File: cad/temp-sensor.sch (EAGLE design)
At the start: 62 parts, among them J2 455-1750-1-ND, Q1 300S14-U, Q2 320S14-U, Q3 320S14-U, U1 SE555D, U2 SE555D, U4 MCP6001UT-I/OT, U5 MCP6001UT-I/OT, U6 MCP6001UT-I/OT, U7 MCP6001UT-I/OT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

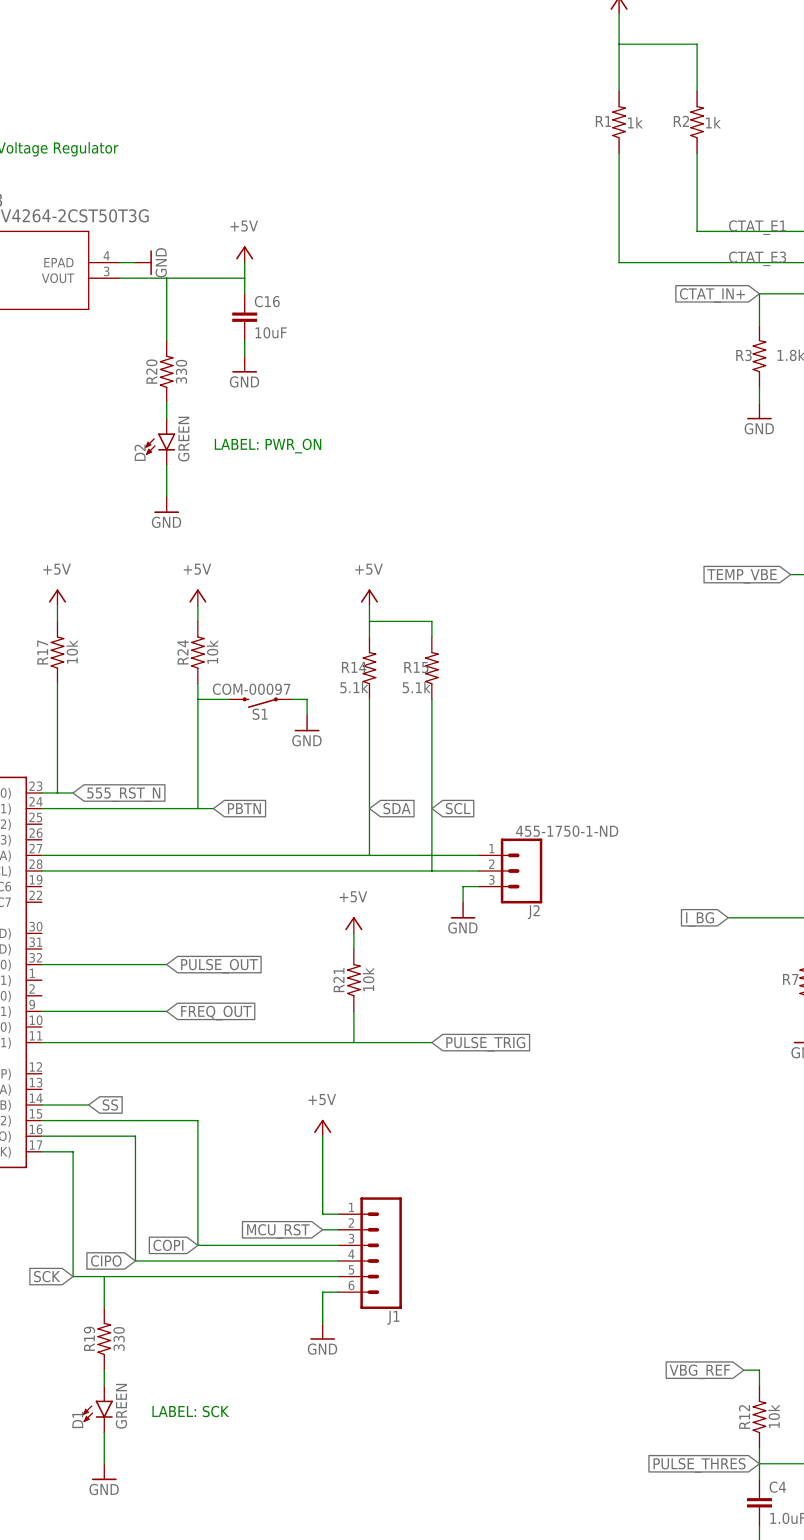
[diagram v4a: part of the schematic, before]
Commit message: Initial routing
Still need to add test points and clean up silk screen.
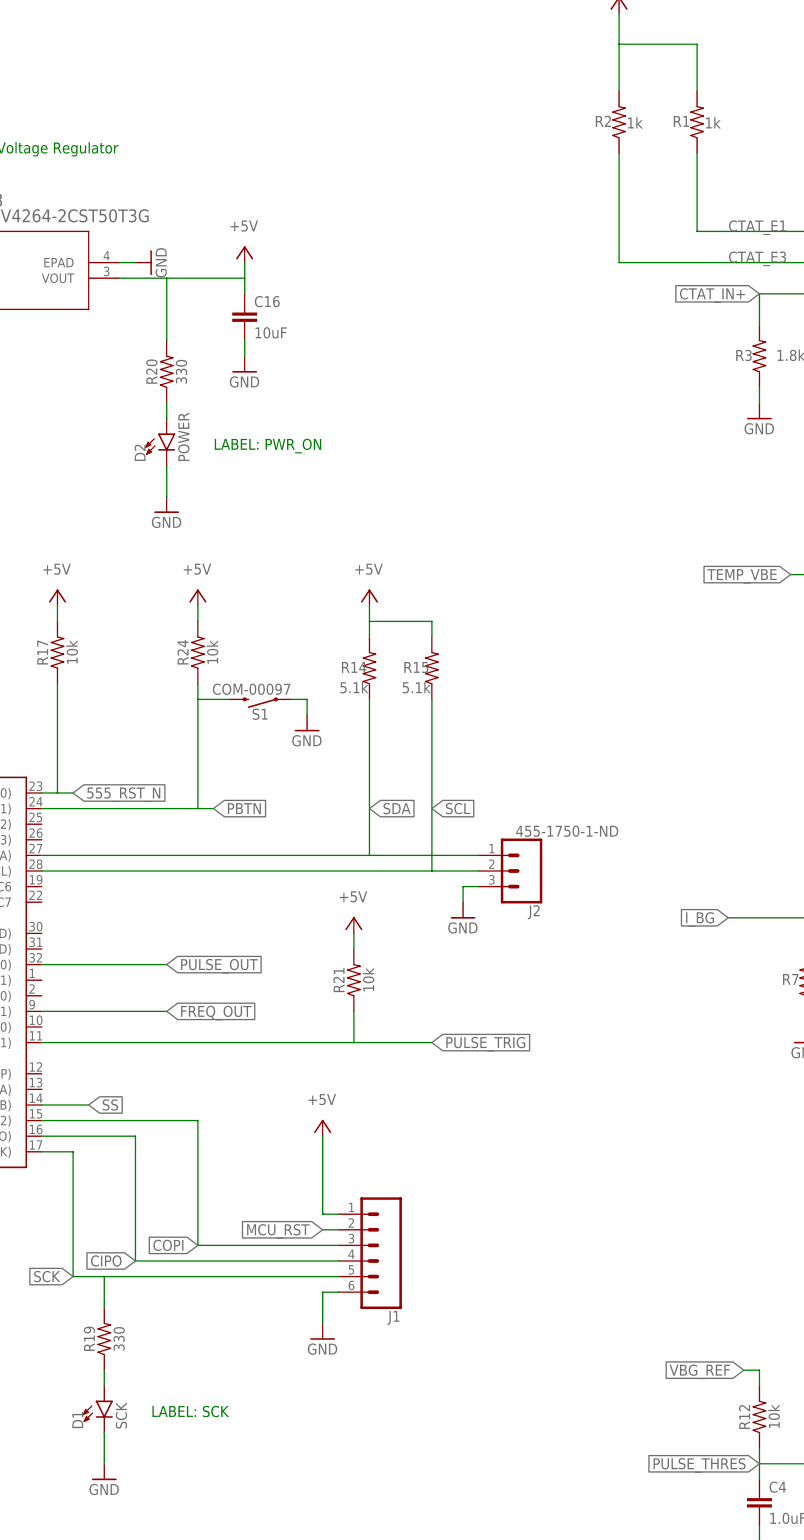
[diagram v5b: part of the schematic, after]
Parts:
- D1: value GREEN -> SCK
- D2: value GREEN -> POWER
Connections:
- net CTAT_E1: now also R1.1; no longer R2.1
- net CTAT_E3: now also R2.1; no longer R1.1
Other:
- moved on the sheet: R1, R2
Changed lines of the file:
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@@
 <part name="P+3" library="supply1" library_urn="urn:adsk.eagle:library:371" deviceset="+5V" device=""/>
 <part name="GND3" library="supply1" library_urn="urn:adsk.eagle:library:371" deviceset="GND" device=""/>
+<part name="R2" library="SparkFun-Resistors" library_urn="urn:adsk.eagle:library:532" deviceset="1KOHM" device="-0603-1/10W-1%" package3d_urn="urn:adsk.eagle:package:41389018/1" value="1k"/>
 <part name="R1" library="SparkFun-Resistors" library_urn="urn:adsk.eagle:library:532" deviceset="1KOHM" device="-0603-1/10W-1%" package3d_urn="urn:adsk.eagle:package:41389018/1" value="1k"/>
-<part name="R2" library="SparkFun-Resistors" library_urn="urn:adsk.eagle:library:532" deviceset="1KOHM" device="-0603-1/10W-1%" package3d_urn="urn:adsk.eagle:package:41389018/1" value="1k"/>
 <part name="R4" library="SparkFun-Resistors" library_urn="urn:adsk.eagle:library:532" deviceset="100KOHM" device="-0603-1/10W-1%" package3d_urn="urn:adsk.eagle:package:41389018/1" value="100k"/>
 <part name="R7" library="SparkFun-Resistors" library_urn="urn:adsk.eagle:library:532" deviceset="5.1KOHM" device="5.1KOHM-0603-1/10W-1%" package3d_urn="urn:adsk.eagle:package:41389018/1" value="5.1k"/>
@@
 <part name="P+17" library="supply1" library_urn="urn:adsk.eagle:library:371" deviceset="+5V" device=""/>
 <part name="P+18" library="supply1" library_urn="urn:adsk.eagle:library:371" deviceset="+5V" device=""/>
-<part name="D1" library="SparkFun-LED" library_urn="urn:adsk.eagle:library:529" deviceset="LED-GREEN" device="1206" package3d_urn="urn:adsk.eagle:package:39352/2" value="GREEN"/>
+<part name="D1" library="SparkFun-LED" library_urn="urn:adsk.eagle:library:529" deviceset="LED-GREEN" device="1206" package3d_urn="urn:adsk.eagle:package:39352/2" value="SCK"/>
 <part name="GND40" library="supply1" library_urn="urn:adsk.eagle:library:371" deviceset="GND" device=""/>
 <part name="R19" library="SparkFun-Resistors" library_urn="urn:adsk.eagle:library:532" deviceset="330OHM" device="-0603-1/10W-1%" package3d_urn="urn:adsk.eagle:package:41389018/1" value="330"/>
-<part name="D2" library="SparkFun-LED" library_urn="urn:adsk.eagle:library:529" deviceset="LED-GREEN" device="1206" package3d_urn="urn:adsk.eagle:package:39352/2" value="GREEN"/>
+<part name="D2" library="SparkFun-LED" library_urn="urn:adsk.eagle:library:529" deviceset="LED-GREEN" device="1206" package3d_urn="urn:adsk.eagle:package:39352/2" value="POWER"/>
 <part name="GND41" library="supply1" library_urn="urn:adsk.eagle:library:371" deviceset="GND" device=""/>
 <part name="R20" library="SparkFun-Resistors" library_urn="urn:adsk.eagle:library:532" deviceset="330OHM" device="-0603-1/10W-1%" package3d_urn="urn:adsk.eagle:package:41389018/1" value="330"/>
@@
 <attribute name="VALUE" x="78.74" y="73.66" size="1.778" layer="96"/>
 </instance>
-<instance part="R1" gate="G$1" x="-22.86" y="243.84" smashed="yes" rot="R90">
+<instance part="R2" gate="G$1" x="-22.86" y="243.84" smashed="yes" rot="R90">
 <attribute name="NAME" x="-25.4" y="244.856" size="1.778" layer="95" font="vector" rot="R180" align="bottom-center"/>
 <attribute name="VALUE" x="-20.32" y="242.824" size="1.778" layer="96" font="vector" rot="R180" align="top-center"/>
 </instance>
-<instance part="R2" gate="G$1" x="-10.16" y="243.84" smashed="yes" rot="R90">
+<instance part="R1" gate="G$1" x="-10.16" y="243.84" smashed="yes" rot="R90">
 <attribute name="NAME" x="-12.7" y="244.856" size="1.778" layer="95" font="vector" rot="R180" align="bottom-center"/>
 <attribute name="VALUE" x="-7.62" y="242.824" size="1.778" layer="96" font="vector" rot="R180" align="top-center"/>
@@
 <wire x1="-22.86" y1="256.54" x2="-22.86" y2="261.62" width="0.1524" layer="91"/>
 <wire x1="-22.86" y1="256.54" x2="-10.16" y2="256.54" width="0.1524" layer="91"/>
+<pinref part="R1" gate="G$1" pin="2"/>
+<wire x1="-10.16" y1="248.92" x2="-10.16" y2="256.54" width="0.1524" layer="91"/>
 <pinref part="R2" gate="G$1" pin="2"/>
-<wire x1="-10.16" y1="248.92" x2="-10.16" y2="256.54" width="0.1524" layer="91"/>
-<pinref part="R1" gate="G$1" pin="2"/>
 <wire x1="-22.86" y1="248.92" x2="-22.86" y2="256.54" width="0.1524" layer="91"/>
 </segment>
@@
 <wire x1="-22.86" y1="220.98" x2="33.02" y2="220.98" width="0.1524" layer="91"/>
 <label x="-5.08" y="220.98" size="1.778" layer="95"/>
-<pinref part="R1" gate="G$1" pin="1"/>
+<pinref part="R2" gate="G$1" pin="1"/>
 </segment>
 </net>
@@
 <wire x1="-10.16" y1="226.06" x2="33.02" y2="226.06" width="0.1524" layer="91"/>
 <label x="-5.08" y="226.06" size="1.778" layer="95"/>
-<pinref part="R2" gate="G$1" pin="1"/>
+<pinref part="R1" gate="G$1" pin="1"/>
 </segment>
 </net>

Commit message: Clean up silk and add test points
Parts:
- added C11, C13: 10uF, SparkFun-Capacitors:10UF-0805-25V-10%
- added TP1, TP2, TP3, TP4: TPPAD1-13, testpad:TPPAD1-13
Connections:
- net +5V: now also TP1.TP
- net GND: now also C11.2, C13.2, TP2.TP
- net VBG_REF: now also C11.1, TP3.TP
- net VPTAT_REF: now also C13.1, TP4.TP
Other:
- note added: "LABEL: POWER"
- note removed: "LABEL: PWR_ON"

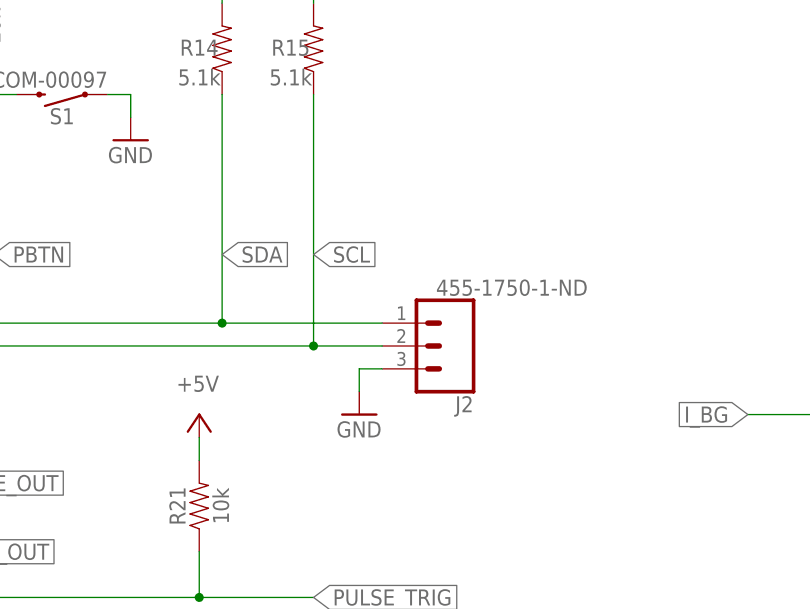
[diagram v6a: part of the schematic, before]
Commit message: Add 4 pin header for OLED
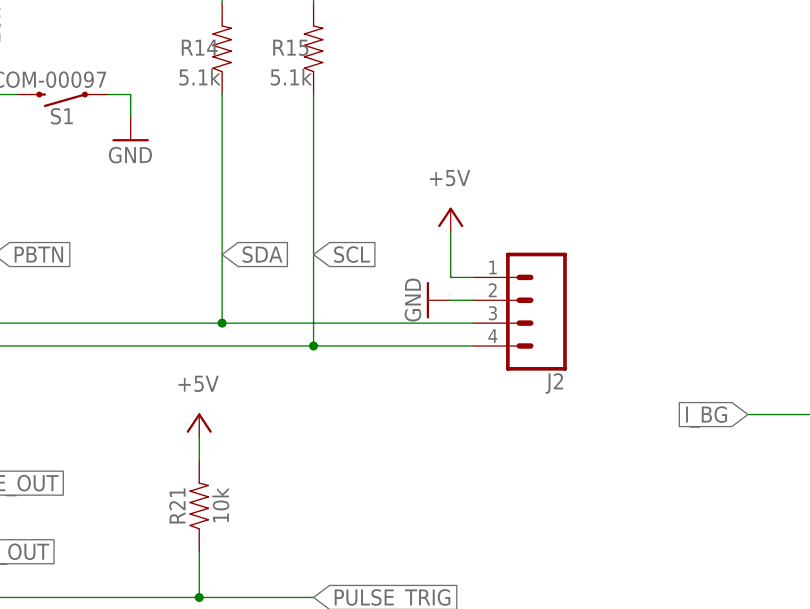
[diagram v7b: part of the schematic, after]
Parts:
- J2: value 455-1750-1-ND -> (none); device SparkFun-Connectors:CONN_03 -> SparkFun-Connectors:CONN_04PTH
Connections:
- net +5V: now also J2.1
- net GND: now also J2.2; no longer J2.3
- net SCL: now also J2.4; no longer J2.2
- net SDA: now also J2.3; no longer J2.1
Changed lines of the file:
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@@
 <part name="P+12" library="supply1" library_urn="urn:adsk.eagle:library:371" deviceset="+5V" device=""/>
 <part name="R21" library="SparkFun-Resistors" library_urn="urn:adsk.eagle:library:532" deviceset="10KOHM" device="-0603-1/10W-1%" package3d_urn="urn:adsk.eagle:package:41389018/1" value="10k"/>
-<part name="J2" library="SparkFun-Connectors" library_urn="urn:adsk.eagle:library:513" deviceset="CONN_03" device="" package3d_urn="urn:adsk.eagle:package:38063/2" value="455-1750-1-ND"/>
 <part name="GND27" library="supply1" library_urn="urn:adsk.eagle:library:371" deviceset="GND" device=""/>
 <part name="C11" library="SparkFun-Capacitors" library_urn="urn:adsk.eagle:library:510" deviceset="10UF" device="-0805-25V-10%" package3d_urn="urn:adsk.eagle:package:41385092/1" value="10uF"/>
@@
 <attribute name="TP_SIGNAL_NAME" value="VPTAT"/>
 </part>
+<part name="J2" library="SparkFun-Connectors" library_urn="urn:adsk.eagle:library:513" deviceset="CONN_04" device="PTH" package3d_urn="urn:adsk.eagle:package:38085/2"/>
+<part name="P+22" library="supply1" library_urn="urn:adsk.eagle:library:371" deviceset="+5V" device=""/>
 </parts>
 <sheets>
@@
 <attribute name="VALUE" x="-64.516" y="104.14" size="1.778" layer="96" font="vector" rot="R90" align="top-center"/>
 </instance>
-<instance part="J2" gate="J1" x="-38.1" y="121.92" smashed="yes" rot="R180">
-<attribute name="VALUE" x="-22.86" y="129.286" size="1.778" layer="96" font="vector" rot="R180"/>
-<attribute name="NAME" x="-35.56" y="116.332" size="1.778" layer="95" font="vector" rot="R180"/>
-</instance>
-<instance part="GND27" gate="1" x="-48.26" y="114.3" smashed="yes">
-<attribute name="VALUE" x="-50.8" y="111.76" size="1.778" layer="96"/>
+<instance part="GND27" gate="1" x="-40.64" y="127" smashed="yes" rot="R270">
+<attribute name="VALUE" x="-43.18" y="129.54" size="1.778" layer="96" rot="R270"/>
 </instance>
 <instance part="C11" gate="G$1" x="91.44" y="106.68" smashed="yes">
@@
 <attribute name="NAME" x="275.59" y="100.33" size="1.778" layer="95" rot="R180"/>
 <attribute name="TP_SIGNAL_NAME" x="278.13" y="102.87" size="1.778" layer="97"/>
+</instance>
+<instance part="J2" gate="J1" x="-30.48" y="127" smashed="yes" rot="R180">
+<attribute name="VALUE" x="-25.4" y="134.366" size="1.778" layer="96" font="vector" rot="R180"/>
+<attribute name="NAME" x="-25.4" y="118.872" size="1.778" layer="95" font="vector" rot="R180"/>
+</instance>
+<instance part="P+22" gate="1" x="-38.1" y="137.16" smashed="yes">
+<attribute name="VALUE" x="-40.64" y="139.7" size="1.778" layer="96"/>
 </instance>
 </instances>
@@
 </segment>
 <segment>
-<wire x1="-48.26" y1="119.38" x2="-48.26" y2="116.84" width="0.1524" layer="91"/>
-<pinref part="GND27" gate="1" pin="GND"/>
-<pinref part="J2" gate="J1" pin="3"/>
-<wire x1="-48.26" y1="119.38" x2="-45.72" y2="119.38" width="0.1524" layer="91"/>
-</segment>
-<segment>
 <pinref part="GND29" gate="1" pin="GND"/>
 <wire x1="91.44" y1="101.6" x2="91.44" y2="104.14" width="0.1524" layer="91"/>
@@
 <wire x1="261.62" y1="101.6" x2="261.62" y2="104.14" width="0.1524" layer="91"/>
 <pinref part="C13" gate="G$1" pin="2"/>
+</segment>
+<segment>
+<pinref part="GND27" gate="1" pin="GND"/>
+<pinref part="J2" gate="J1" pin="2"/>
+<wire x1="-38.1" y1="127" x2="-35.56" y2="127" width="0.1524" layer="91"/>
 </segment>
 </net>
@@
 <wire x1="-66.04" y1="111.76" x2="-66.04" y2="109.22" width="0.1524" layer="91"/>
 </segment>
+<segment>
+<pinref part="J2" gate="J1" pin="1"/>
+<wire x1="-35.56" y1="129.54" x2="-38.1" y2="129.54" width="0.1524" layer="91"/>
+<wire x1="-38.1" y1="129.54" x2="-38.1" y2="134.62" width="0.1524" layer="91"/>
+<pinref part="P+22" gate="1" pin="+5V"/>
+</segment>
 </net>
 <net name="CTAT_BASE" class="0">
@@
 <wire x1="-116.84" y1="124.46" x2="-63.5" y2="124.46" width="0.1524" layer="91"/>
 <label x="-63.5" y="132.08" size="1.778" layer="95" xref="yes"/>
-<wire x1="-63.5" y1="124.46" x2="-45.72" y2="124.46" width="0.1524" layer="91"/>
+<wire x1="-63.5" y1="124.46" x2="-35.56" y2="124.46" width="0.1524" layer="91"/>
 <wire x1="-63.5" y1="124.46" x2="-63.5" y2="149.86" width="0.1524" layer="91"/>
 <pinref part="R14" gate="R1" pin="1"/>
-<pinref part="J2" gate="J1" pin="1"/>
 <junction x="-63.5" y="124.46"/>
+<pinref part="J2" gate="J1" pin="3"/>
 </segment>
 </net>
@@
 <wire x1="-53.34" y1="121.92" x2="-53.34" y2="149.86" width="0.1524" layer="91"/>
 <pinref part="R15" gate="R1" pin="1"/>
-<wire x1="-53.34" y1="121.92" x2="-45.72" y2="121.92" width="0.1524" layer="91"/>
-<pinref part="J2" gate="J1" pin="2"/>
 <junction x="-53.34" y="121.92"/>
-</segment>
-</net>
+<pinref part="J2" gate="J1" pin="4"/>
+<wire x1="-53.34" y1="121.92" x2="-35.56" y2="121.92" width="0.1524" layer="91"/>
+</segment>
+</net>
